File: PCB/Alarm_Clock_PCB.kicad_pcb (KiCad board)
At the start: 2 copper layers, 87.5 x 46 mm, 12 parts, among them J1 Conn_01x08_Pin, SW1 SW_Push, SW2 SW_Push, SW3 SW_Push, SW4 SW_Push, U1 XIAO-ESP32-C3-SMD

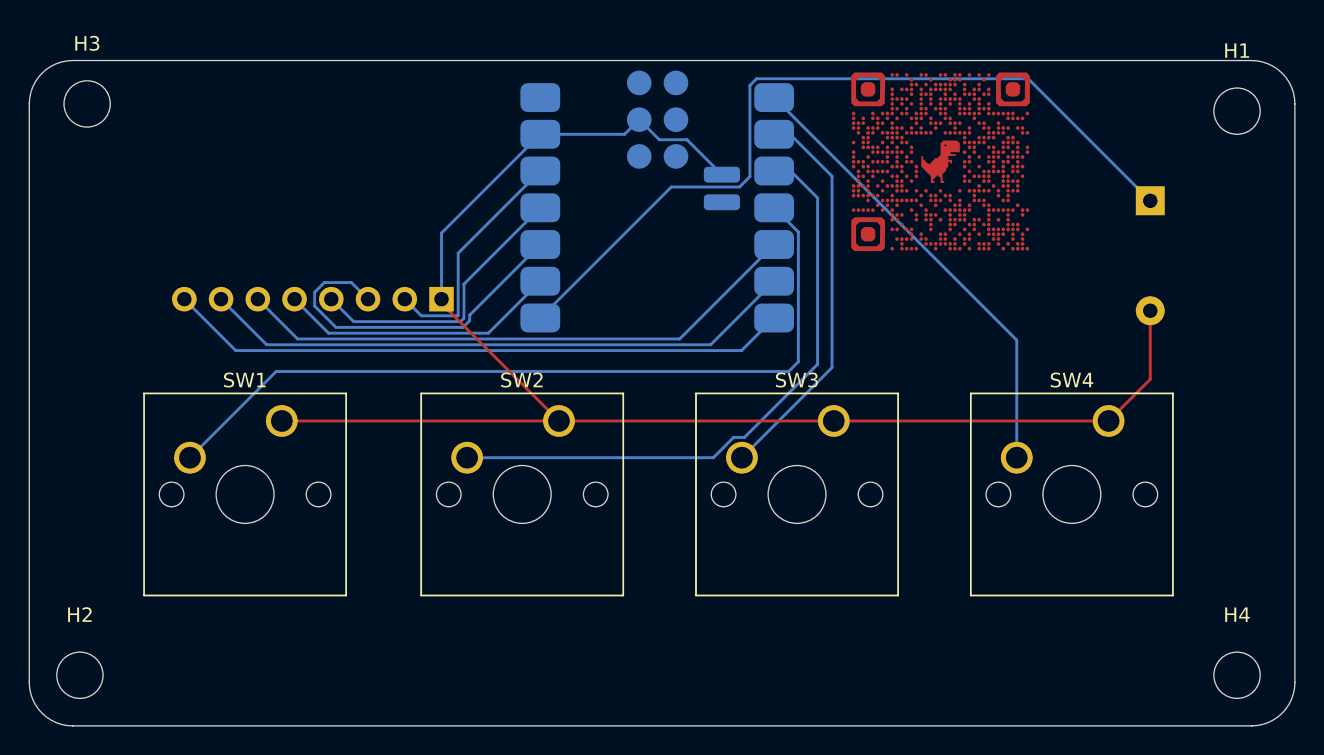
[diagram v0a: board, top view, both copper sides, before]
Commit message: Changed PCB from SMD to DIP soldering
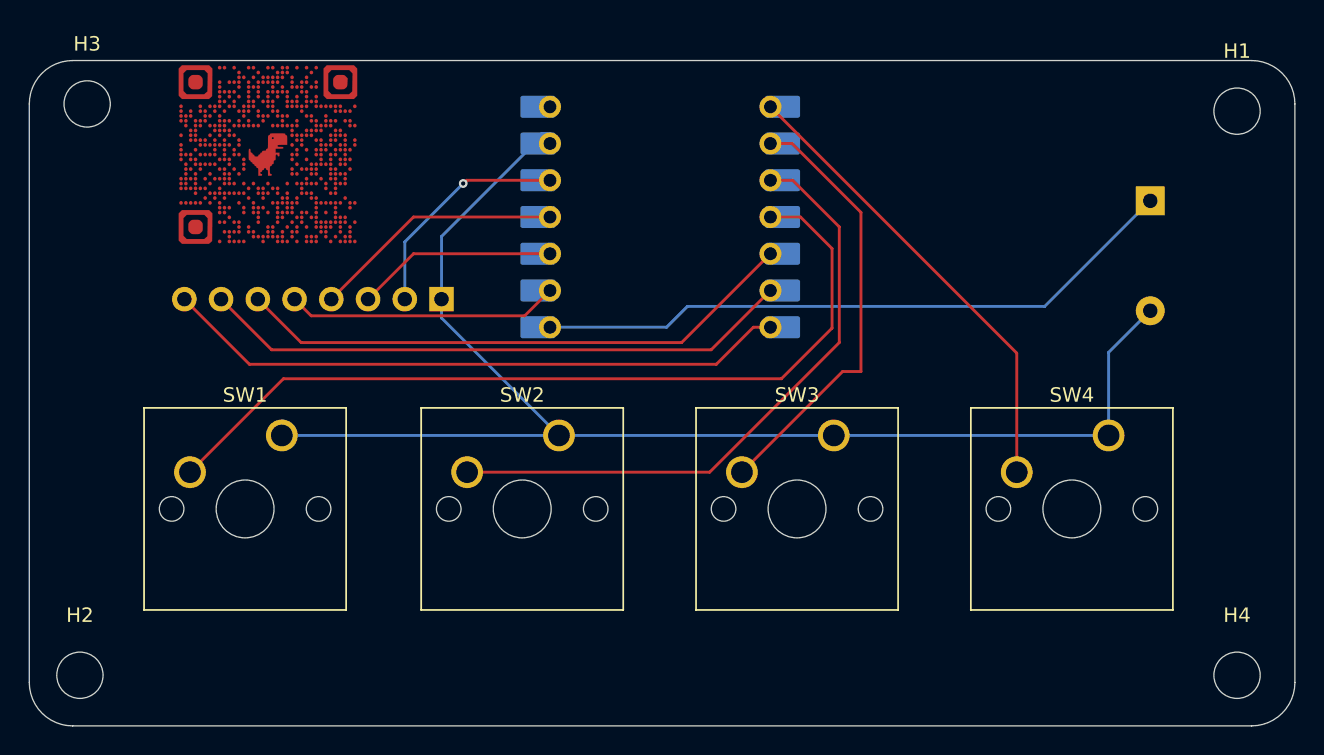
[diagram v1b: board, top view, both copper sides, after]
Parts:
- U1: footprint Seeed_Studio_XIAO_Series:XIAO-ESP32-C3-SMD -> Seeed_Studio_XIAO_Series:XIAO-ESP32-C3-DIP
- moved G*** 46.5 mm to (153.5, 102.5)
- moved U1 13.2 mm to (180.6, 106.8), turned to 90 degrees
- moved SW1 1.00 mm to (154.5, 121.9)
- moved SW2 1.00 mm to (173.6, 121.9)
- moved SW3 1.00 mm to (192.6, 121.9)
- moved SW4 1.00 mm to (211.6, 121.9)
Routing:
- net GND: track 106.5 -> 95.1 mm
- net Net-(BZ1-+): track 56.2 -> 45.1 mm
- net /SCL: track 24.2 -> 13.9 mm
- net Net-(U1-D1): track 27.2 -> 30.3 mm
- net Net-(U1-D3): track 56.2 -> 59.2 mm
- net /SDA: track 19.7 -> 17.5 mm
- net Net-(U1-D2): track 42.2 -> 43.5 mm
- net +3.3V: track 16.5 -> 15.8 mm, vias 0 -> 1
- net /RST: track 19.5 -> 18.9 mm
